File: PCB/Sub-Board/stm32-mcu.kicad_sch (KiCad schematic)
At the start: 90 parts, among them J34 Conn_01x04_Pin, U2 74HC165, U3 STM32F401VETx, U4 74HC165, U5 74HC165, U6 74HC165, U7 74HC165, Y1 26 MHz

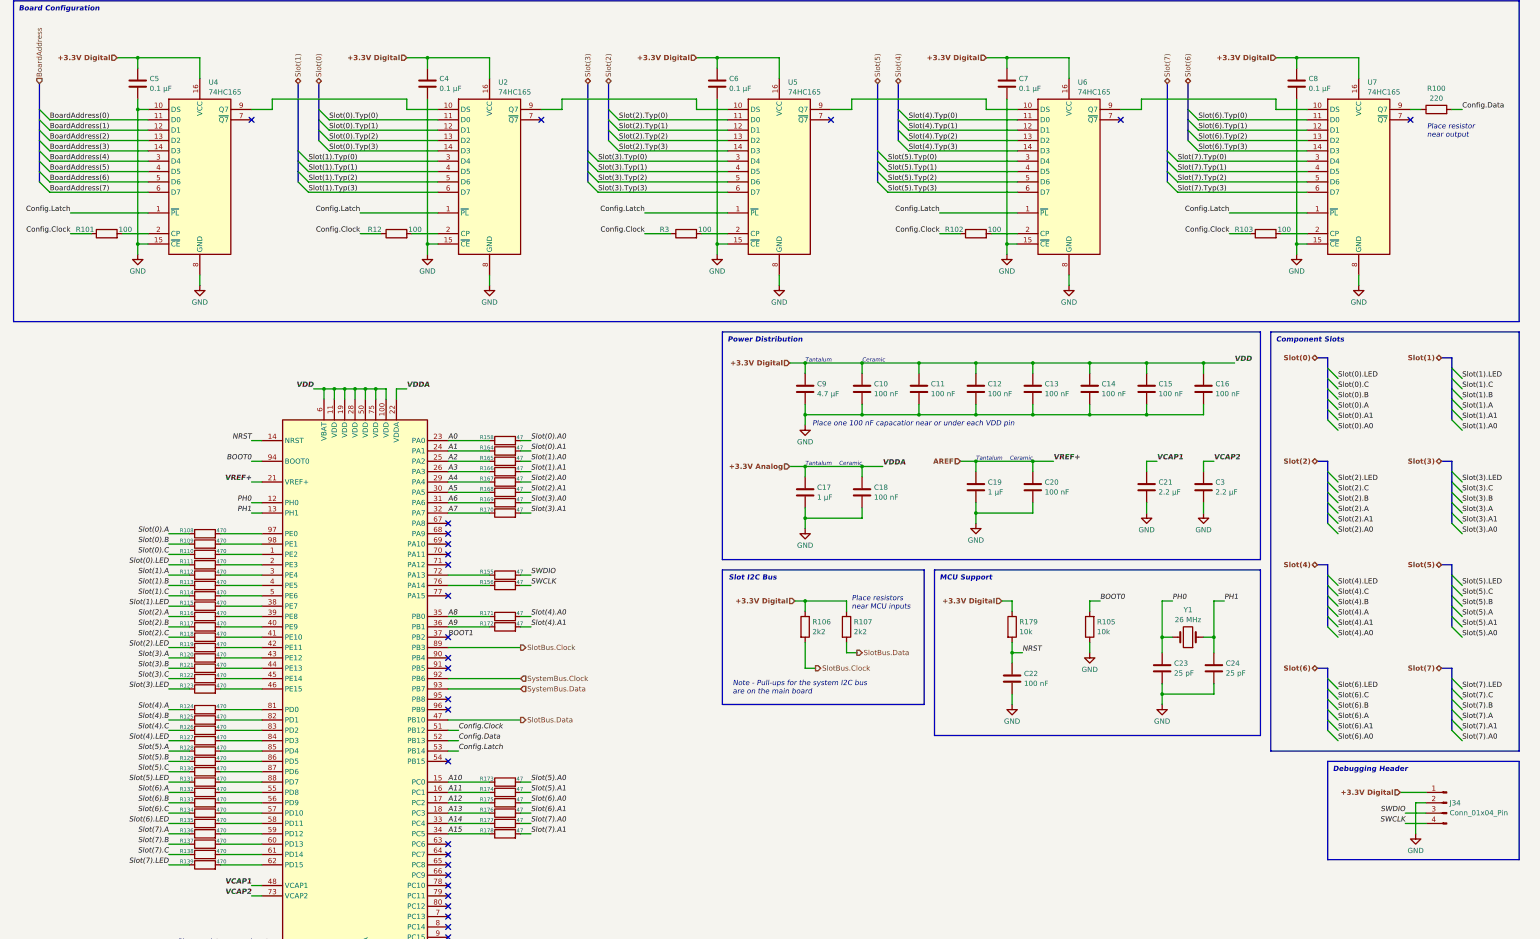
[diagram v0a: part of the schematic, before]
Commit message: Sub-Board PCB before ERC
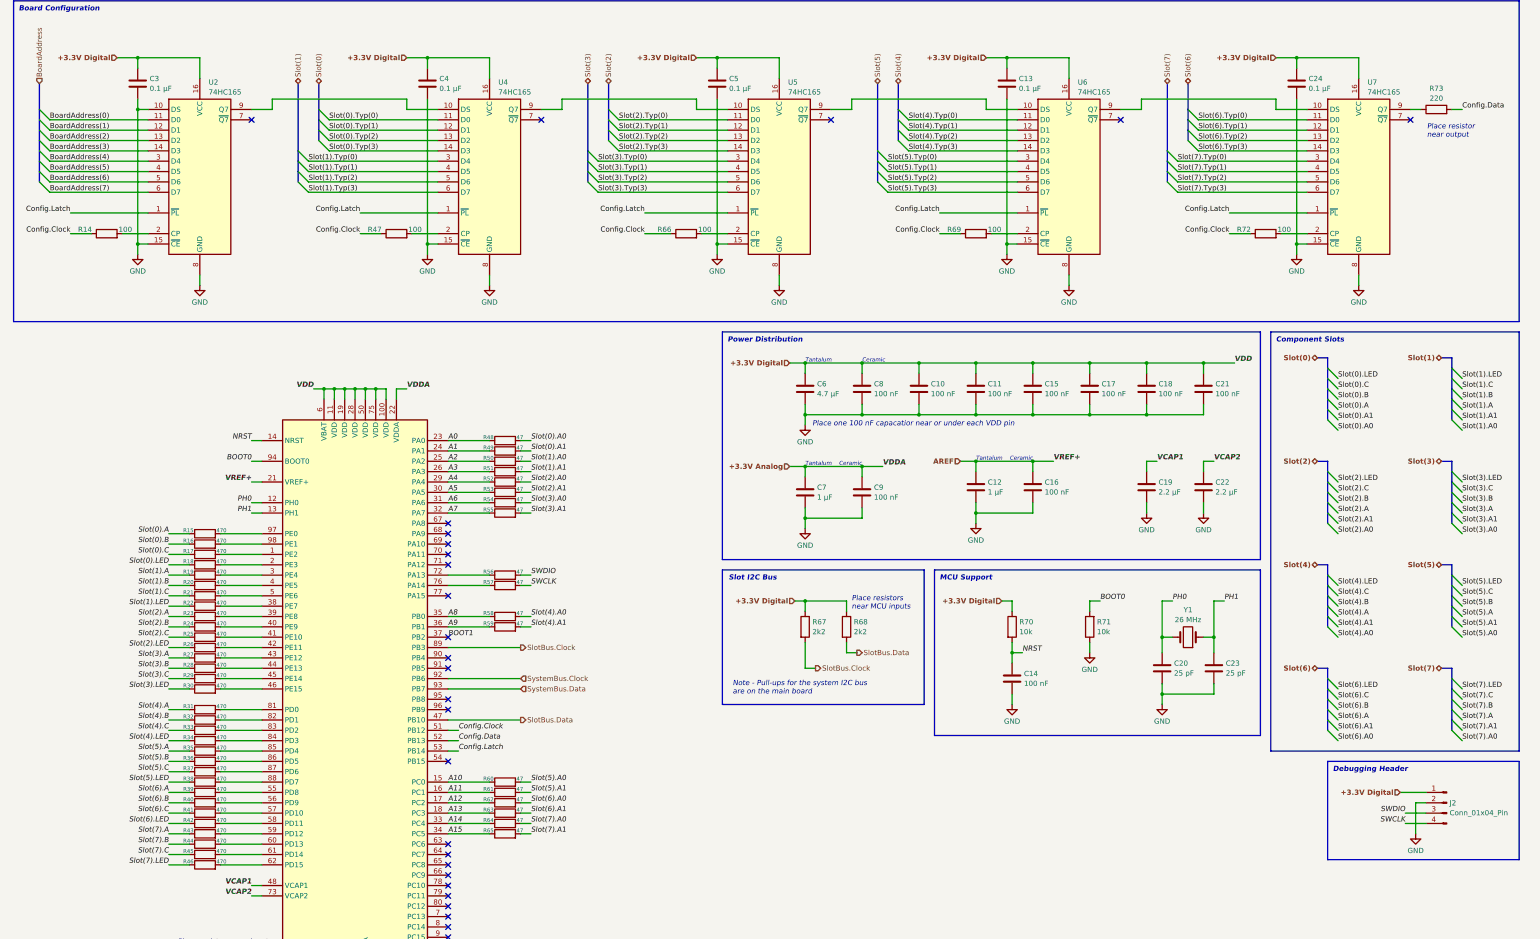
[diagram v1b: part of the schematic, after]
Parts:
- renumbered C11 to C10, C12 to C11, C19 to C12, C7 to C13, C22 to C14, C13 to C15, C20 to C16, C14 to C17, C15 to C18, C21 to C19, C23 to C20, C16 to C21, C3 to C22, C24 to C23, C8 to C24, C5 to C3, C6 to C5, C9 to C6, C17 to C7, C10 to C8, C18 to C9, J34 to J2, R101 to R14, R108 to R15, R109 to R16, R110 to R17, R111 to R18, R112 to R19, R113 to R20, R114 to R21, R115 to R22, R116 to R23, R117 to R24, R118 to R25, R119 to R26, R120 to R27, R121 to R28, R122 to R29, R123 to R30, R124 to R31, R125 to R32, R126 to R33, R127 to R34, R128 to R35, R129 to R36, R130 to R37, R131 to R38, R132 to R39, R133 to R40, R134 to R41, R135 to R42, R136 to R43, R137 to R44, R138 to R45, R139 to R46, R12 to R47, R158 to R48, R164 to R49, R165 to R50, R166 to R51, R167 to R52, R168 to R53, R169 to R54, R170 to R55, R155 to R56, R156 to R57, R171 to R58, R172 to R59, R173 to R60, R174 to R61, R175 to R62, R176 to R63, R177 to R64, R178 to R65, R3 to R66, R106 to R67, R107 to R68, R102 to R69, R179 to R70, R105 to R71, R103 to R72, R100 to R73, U4 to U2, U2 to U4

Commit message: Sub-Board PCB after ERC
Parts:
- renumbered C9 to C10, C10 to C11, C11 to C12, C12 to C13, C24 to C17, C17 to C18, C18 to C19, C19 to C20, C20 to C21, C21 to C22, C22 to C23, C23 to C24, C13 to C6, C6 to C7, C7 to C8, C8 to C9, R69 to R67, R67 to R68, R68 to R69, R72 to R70, R70 to R71, R71 to R72
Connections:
- net BoardAddress(0) renamed BoardAddress0
- net BoardAddress(1) renamed BoardAddress1
- net BoardAddress(2) renamed BoardAddress2
- net BoardAddress(3) renamed BoardAddress3
- net BoardAddress(4) renamed BoardAddress4
- net BoardAddress(5) renamed BoardAddress5
- net BoardAddress(6) renamed BoardAddress6
- net BoardAddress(7) renamed BoardAddress7
- net Slot(0).A renamed Slot0.A
- net Slot(0).A0 renamed Slot0.A0
- net Slot(0).A1 renamed Slot0.A1
- net Slot(0).B renamed Slot0.B
- net Slot(0).C renamed Slot0.C
- net Slot(0).LED renamed Slot0.LED
- net Slot(0).Typ(0) renamed Slot0.Typ0
- net Slot(0).Typ(1) renamed Slot0.Typ1
- net Slot(0).Typ(2) renamed Slot0.Typ2
- net Slot(0).Typ(3) renamed Slot0.Typ3
- net Slot(1).A renamed Slot1.A
- net Slot(1).A0 renamed Slot1.A0
- net Slot(1).A1 renamed Slot1.A1
- net Slot(1).B renamed Slot1.B
- net Slot(1).C renamed Slot1.C
- net Slot(1).LED renamed Slot1.LED
- net Slot(1).Typ(0) renamed Slot1.Typ0
- net Slot(1).Typ(1) renamed Slot1.Typ1
- net Slot(1).Typ(2) renamed Slot1.Typ2
- net Slot(1).Typ(3) renamed Slot1.Typ3
- net Slot(2).A renamed Slot2.A
- net Slot(2).A0 renamed Slot2.A0
- net Slot(2).A1 renamed Slot2.A1
- net Slot(2).B renamed Slot2.B
- net Slot(2).C renamed Slot2.C
- net Slot(2).LED renamed Slot2.LED
- net Slot(2).Typ(0) renamed Slot2.Typ0
- net Slot(2).Typ(1) renamed Slot2.Typ1
- net Slot(2).Typ(2) renamed Slot2.Typ2
- net Slot(2).Typ(3) renamed Slot2.Typ3
- net Slot(3).A renamed Slot3.A
- net Slot(3).A0 renamed Slot3.A0
- net Slot(3).A1 renamed Slot3.A1
- net Slot(3).B renamed Slot3.B
- net Slot(3).C renamed Slot3.C
- net Slot(3).LED renamed Slot3.LED
- net Slot(3).Typ(0) renamed Slot3.Typ0
- net Slot(3).Typ(1) renamed Slot3.Typ1
- net Slot(3).Typ(2) renamed Slot3.Typ2
- net Slot(3).Typ(3) renamed Slot3.Typ3
- net Slot(4).A renamed Slot4.A
- net Slot(4).A0 renamed Slot4.A0
- net Slot(4).A1 renamed Slot4.A1
- net Slot(4).B renamed Slot4.B
- net Slot(4).C renamed Slot4.C
- net Slot(4).LED renamed Slot4.LED
- net Slot(4).Typ(0) renamed Slot4.Typ0
- net Slot(4).Typ(1) renamed Slot4.Typ1
- net Slot(4).Typ(2) renamed Slot4.Typ2
- net Slot(4).Typ(3) renamed Slot4.Typ3
- net Slot(5).A renamed Slot5.A
- net Slot(5).A0 renamed Slot5.A0
- net Slot(5).A1 renamed Slot5.A1
- net Slot(5).B renamed Slot5.B
- net Slot(5).C renamed Slot5.C
- net Slot(5).LED renamed Slot5.LED
- net Slot(5).Typ(0) renamed Slot5.Typ0
- net Slot(5).Typ(1) renamed Slot5.Typ1
- net Slot(5).Typ(2) renamed Slot5.Typ2
- net Slot(5).Typ(3) renamed Slot5.Typ3
- net Slot(6).A renamed Slot6.A
- net Slot(6).A0 renamed Slot6.A0
- net Slot(6).A1 renamed Slot6.A1
- net Slot(6).B renamed Slot6.B
- net Slot(6).C renamed Slot6.C
- net Slot(6).LED renamed Slot6.LED
- net Slot(6).Typ(0) renamed Slot6.Typ0
- net Slot(6).Typ(1) renamed Slot6.Typ1
- net Slot(6).Typ(2) renamed Slot6.Typ2
- net Slot(6).Typ(3) renamed Slot6.Typ3
- net Slot(7).A renamed Slot7.A
- net Slot(7).A0 renamed Slot7.A0
- net Slot(7).A1 renamed Slot7.A1
- net Slot(7).B renamed Slot7.B
- net Slot(7).C renamed Slot7.C
- net Slot(7).LED renamed Slot7.LED
- net Slot(7).Typ(0) renamed Slot7.Typ0
- net Slot(7).Typ(1) renamed Slot7.Typ1
- net Slot(7).Typ(2) renamed Slot7.Typ2
- net Slot(7).Typ(3) renamed Slot7.Typ3
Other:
- note removed: "Component Slots"
- moved on the sheet: C10, C11, C12, C13, C14, C15, C16, C17, C18, C19, C20, C21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

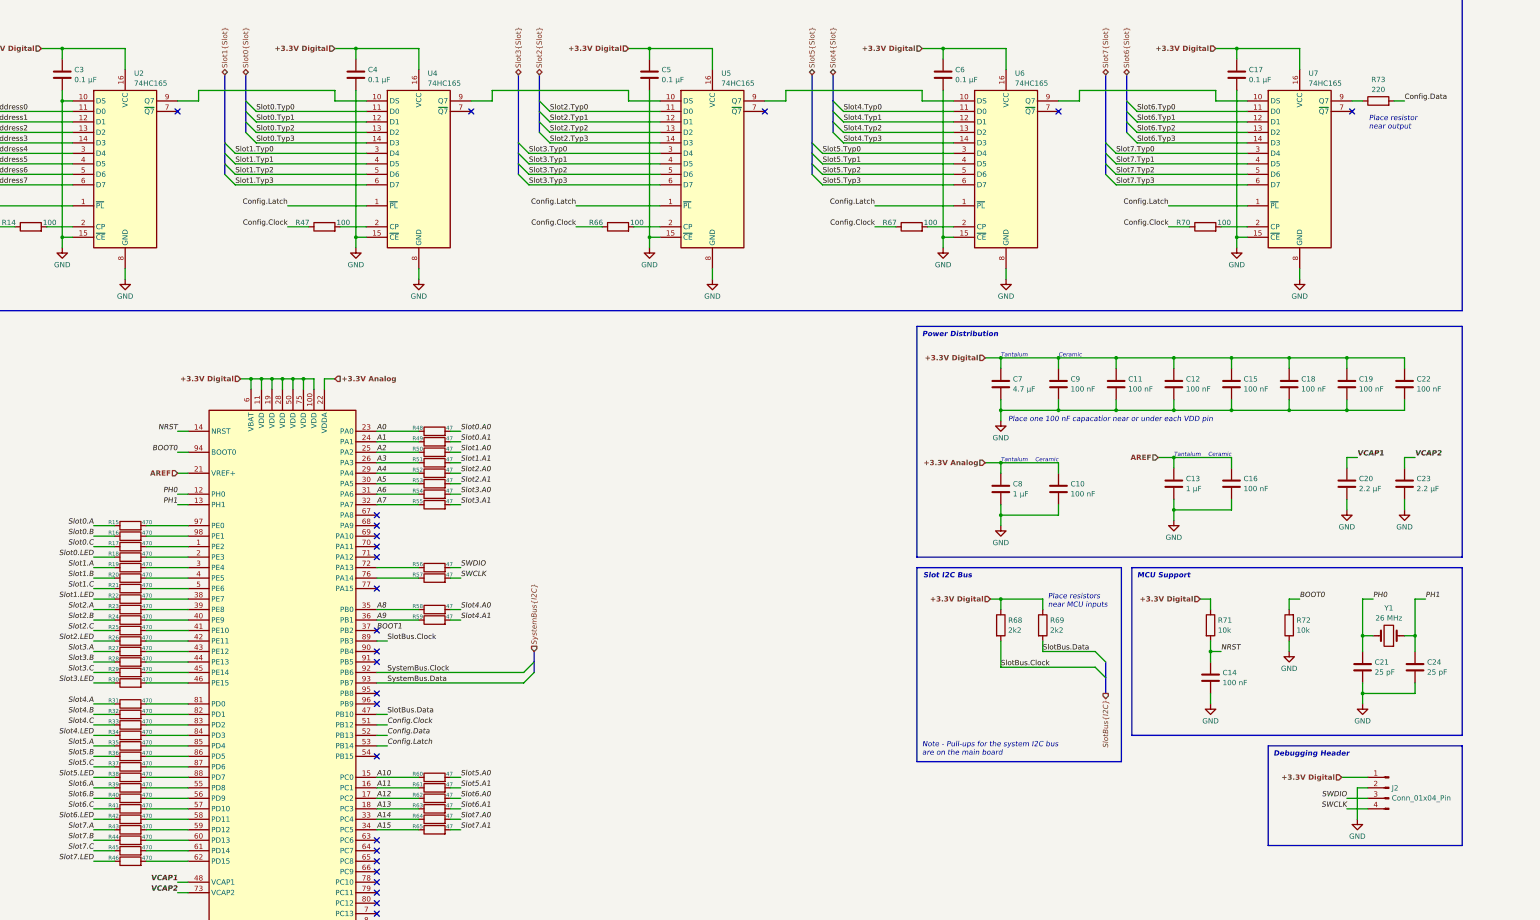
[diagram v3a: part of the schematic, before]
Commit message: Sub-Board PCB: Footprint assignments
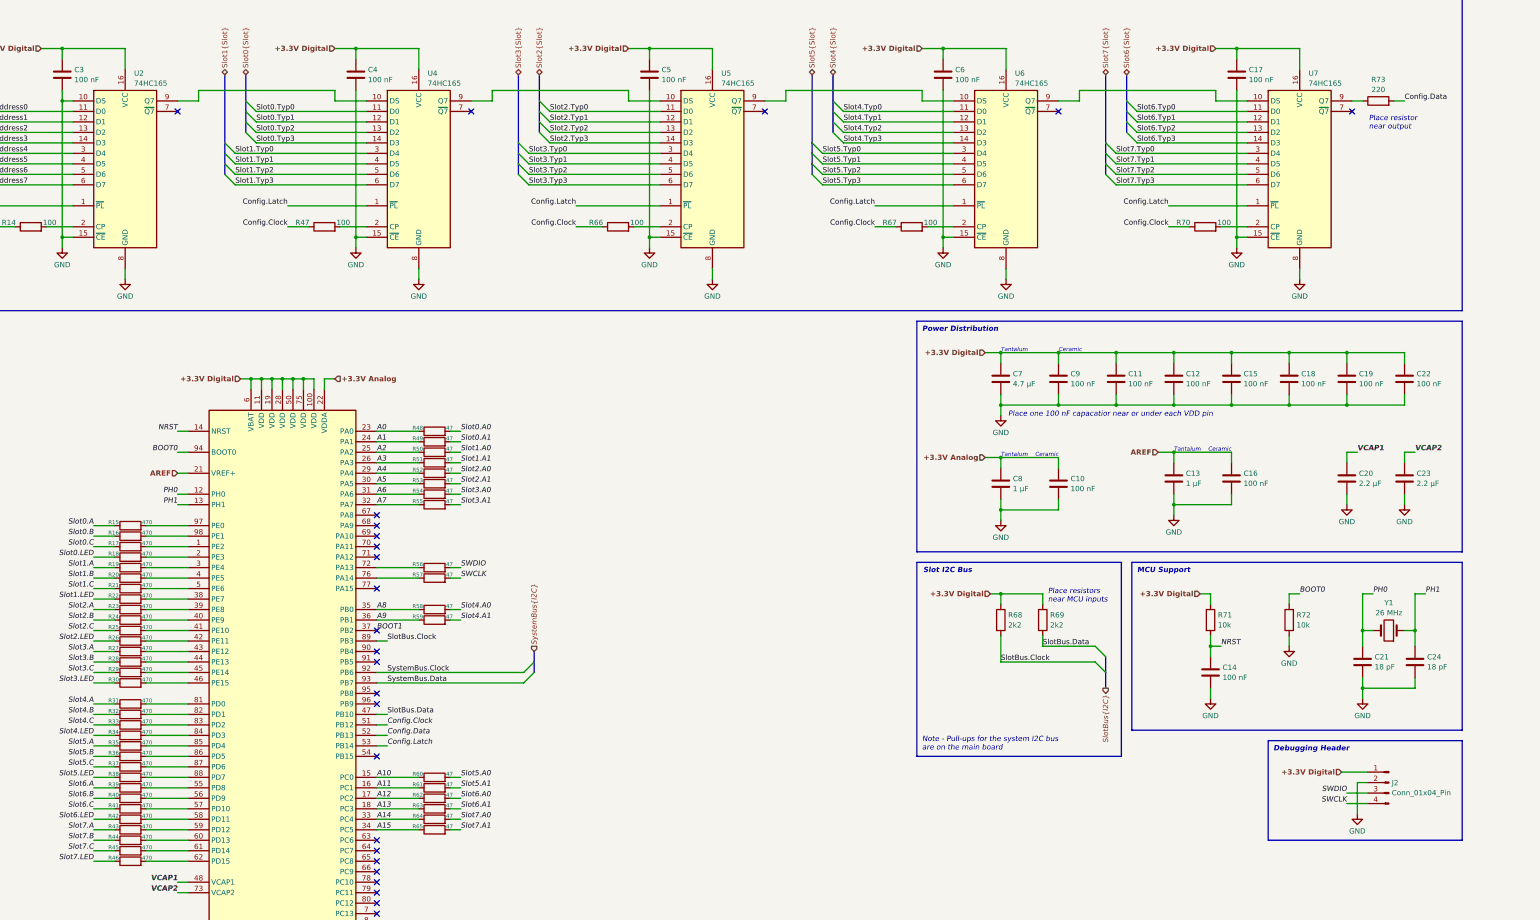
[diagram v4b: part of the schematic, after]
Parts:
- C10, C11, C12, C14, C15, C16, C18, C19, C22, C9: footprint (none) -> Capacitor_SMD:C_0603_1608Metric
- C13, C20, C23, C7, C8: footprint (none) -> Capacitor_SMD:C_0805_2012Metric
- C17, C3, C4, C5, C6: value 0.1 µF -> 100 nF; footprint (none) -> Capacitor_SMD:C_0603_1608Metric
- C21, C24: value 25 pF -> 18 pF; footprint (none) -> Capacitor_SMD:C_0603_1608Metric
- J2: footprint (none) -> Connector_PinHeader_2.54mm:PinHeader_1x04_P2.54mm_Vertical
- R14, R15, R16, R17, R18, R19, R20, R21, R22, R23, R24, R25, R26, R27, R28, R29, R30, R31, R32, R33, R34, R35, R36, R37, R38, R39, R40, R41, R42, R43, R44, R45, R46, R47, R48, R49, R50, R51, R52, R53, R54, R55, R56, R57, R58, R59, R60, R61, R62, R63, R64, R65, R66, R67, R68, R69, R70, R71, R72, R73: footprint (none) -> Resistor_SMD:R_0603_1608Metric
- U2, U4, U5, U6, U7: footprint (none) -> Package_SO:TSSOP-16_4.4x5mm_P0.65mm
- Y1: footprint (none) -> Crystal:Crystal_SMD_3215-2Pin_3.2x1.5mm
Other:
- title: Modular Music Controller – STM32 MCU (Controller Logic) -> Modular Music Controller / Sub-Board / STM32 MCU
- moved on the sheet: C10, C11, C12, C13, C14, C15, C16, C18, C19, C20, C21, C22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

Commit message: Sub Board PCB: PCB Layout (wip)
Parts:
- removed R15, R16, R17, R18, R19, R20, R21, R22, R23, R24, R25, R26, R27, R28, R29, R30, R31, R32, R33, R34, R35, R36, R37, R38, R39, R40, R41, R42, R43, R44, R45, R46: 470, Resistor_SMD:R_0603_1608Metric, symbol Device:R
- removed R48, R49, R50, R51, R52, R53, R54, R55, R58, R59, R60, R61, R62, R63, R64, R65: 47, Resistor_SMD:R_0603_1608Metric, symbol Device:R
- R14: footprint Resistor_SMD:R_0603_1608Metric -> Resistor_SMD:R_0402_1005Metric
- R15: renamed from R47; footprint Resistor_SMD:R_0603_1608Metric -> Resistor_SMD:R_0402_1005Metric
- R16: renamed from R56; footprint Resistor_SMD:R_0603_1608Metric -> Resistor_SMD:R_0402_1005Metric
- R17: renamed from R57; footprint Resistor_SMD:R_0603_1608Metric -> Resistor_SMD:R_0402_1005Metric
- R18: renamed from R66; footprint Resistor_SMD:R_0603_1608Metric -> Resistor_SMD:R_0402_1005Metric
- R19: renamed from R67; footprint Resistor_SMD:R_0603_1608Metric -> Resistor_SMD:R_0402_1005Metric
- R20: renamed from R68; footprint Resistor_SMD:R_0603_1608Metric -> Resistor_SMD:R_0402_1005Metric
- R21: renamed from R69; footprint Resistor_SMD:R_0603_1608Metric -> Resistor_SMD:R_0402_1005Metric
- R22: renamed from R70; footprint Resistor_SMD:R_0603_1608Metric -> Resistor_SMD:R_0402_1005Metric
- R23: renamed from R71; footprint Resistor_SMD:R_0603_1608Metric -> Resistor_SMD:R_0402_1005Metric
- R24: renamed from R72; footprint Resistor_SMD:R_0603_1608Metric -> Resistor_SMD:R_0402_1005Metric
- R25: renamed from R73; footprint Resistor_SMD:R_0603_1608Metric -> Resistor_SMD:R_0402_1005Metric
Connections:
- net A0 is gone; now on net Slot0.A0: U3.23 (PA0)
- net A1 is gone; now on net Slot0.A1: U3.24 (PA1)
- net A10 is gone; now on net Slot5.A0: U3.15 (PC0)
- net A11 is gone; now on net Slot5.A1: U3.16 (PC1)
- net A12 is gone; now on net Slot6.A0: U3.17 (PC2)
- net A13 is gone; now on net Slot6.A1: U3.18 (PC3)
- net A14 is gone; now on net Slot7.A0: U3.33 (PC4)
- net A15 is gone; now on net Slot7.A1: U3.34 (PC5)
- net A2 is gone; now on net Slot1.A0: U3.25 (PA2)
- net A3 is gone; now on net Slot1.A1: U3.26 (PA3)
- net A4 is gone; now on net Slot2.A0: U3.29 (PA4)
- net A5 is gone; now on net Slot2.A1: U3.30 (PA5)
- net A6 is gone; now on net Slot3.A0: U3.31 (PA6)
- net A7 is gone; now on net Slot3.A1: U3.32 (PA7)
- net A8 is gone; now on net Slot4.A0: U3.35 (PB0)
- net A9 is gone; now on net Slot4.A1: U3.36 (PB1)
- net Slot0.A: now also U3.97 (PE0)
- net Slot0.B: now also U3.98 (PE1)
- net Slot0.C: now also U3.1 (PE2)
- net Slot0.LED: now also U3.2 (PE3)
- net Slot1.A: now also U3.3 (PE4)
- net Slot1.B: now also U3.4 (PE5)
- net Slot1.C: now also U3.5 (PE6)
- net Slot1.LED: now also U3.38 (PE7)
- net Slot2.A: now also U3.39 (PE8)
- net Slot2.B: now also U3.40 (PE9)
- net Slot2.C: now also U3.41 (PE10)
- net Slot2.LED: now also U3.42 (PE11)
- net Slot3.A: now also U3.43 (PE12)
- net Slot3.B: now also U3.44 (PE13)
- net Slot3.C: now also U3.45 (PE14)
- net Slot3.LED: now also U3.46 (PE15)
- net Slot4.A: now also U3.81 (PD0)
- net Slot4.B: now also U3.82 (PD1)
- net Slot4.C: now also U3.83 (PD2)
- net Slot4.LED: now also U3.84 (PD3)
- net Slot5.A: now also U3.85 (PD4)
- net Slot5.B: now also U3.86 (PD5)
- net Slot5.C: now also U3.87 (PD6)
- net Slot5.LED: now also U3.88 (PD7)
- net Slot6.A: now also U3.55 (PD8)
- net Slot6.B: now also U3.56 (PD9)
- net Slot6.C: now also U3.57 (PD10)
- net Slot6.LED: now also U3.58 (PD11)
- net Slot7.A: now also U3.59 (PD12)
- net Slot7.B: now also U3.60 (PD13)
- net Slot7.C: now also U3.61 (PD14)
- net Slot7.LED: now also U3.62 (PD15)
- net BOOT1: no longer names the net of U3.37 (PB2)
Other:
- note added: "A0"
- note added: "A1"
- note added: "A10"
- note added: "A11"
- note added: "A12"
- note added: "A13"
- note added: "A14"
- note added: "A15"
- note added: "A2"
- note added: "A3"
- note added: "A4"
- note added: "A5"
- note added: "A6"
- note added: "A7"
- note added: "A8"
- note added: "A9"
- note added: "BOOT1"
- note removed: "Place resistors near input to protect against noise"

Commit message: Sub Board PCB: Parts Placement (wip)
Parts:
- J2: footprint Connector_PinHeader_2.54mm:PinHeader_1x04_P2.54mm_Vertical -> Connector_PinHeader_2.54mm:PinHeader_1x04_P2.54mm_Vertical_SMD_Pin1Right
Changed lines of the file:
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@@
 			)
 		)
-		(property "Footprint" "Connector_PinHeader_2.54mm:PinHeader_1x04_P2.54mm_Vertical"
+		(property "Footprint" "Connector_PinHeader_2.54mm:PinHeader_1x04_P2.54mm_Vertical_SMD_Pin1Right"
 			(at 384.81 222.25 0)
 			(effects
